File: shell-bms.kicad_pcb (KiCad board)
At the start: 4 copper layers, 184 parts, among them J1 Conn_01x20, J10 Conn_01x05, J11 USB_C_Receptacle_USB2.0_16P, J13 OUTSIDE LED, J2 Conn_01x20, J3 Conn_01x04, J4 Output, J5 USB_C_Receptacle_USB2.0_16P, J6 Conn_01x02, J7 Conn_01x02, J8 Conn_01x02, J9 Conn_01x04, Q1 NPN, Q2 HY3610P, Q3 HY3610P, Q4 BC817, Q5 BC817, Q6 BC817, SW1 SW_Push, SW2 SW_Nidec_CAS-120A1, U1 BQ76952PFBR, U2 LM5017MR, U3 STM32G431C8Tx, U4 AP2204K-5.0, U5 CH340K, U6 XC6206 - 3V3, U7 ESP-WROOM-02, U8 TJA1051T, U9 CH340K, Y1 8MHz

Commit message: finalised product
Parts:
- added Q7: BC817, Package_TO_SOT_SMD:SOT-23, F.Cu at (182.2, 161.2)
- added R72: 260, Resistor_SMD:R_0603_1608Metric_Pad0.98x0.95mm_HandSolder, F.Cu at (181.2, 164.8)
- C10, C11, C12, C13, C14, C15, C16, C17, C2, C3, C4, C42, C43, C45, C47, C5, C52, C53, C54, C59, C6, C60, C7, C8, C9: moved to B.Cu
- JP1: footprint Connector_PinHeader_1.27mm:PinHeader_1x03_P1.27mm_Horizontal -> Connector_PinHeader_1.27mm:PinHeader_1x03_P1.27mm_Vertical
- R18, R19, R20, R21: footprint Resistor_SMD:R_1210_3225Metric_Pad1.30x2.65mm_HandSolder -> Resistor_SMD:R_0603_1608Metric_Pad0.98x0.95mm_HandSolder
- R25, R26, R27, R39: footprint Resistor_THT:R_Axial_DIN0309_L9.0mm_D3.2mm_P15.24mm_Horizontal -> Resistor_SMD:R_1210_3225Metric_Pad1.30x2.65mm_HandSolder
- R31, R37, R38: footprint Resistor_THT:R_Axial_DIN0309_L9.0mm_D3.2mm_P15.24mm_Horizontal -> Resistor_SMD:R_1206_3216Metric
- R60: footprint Resistor_SMD:R_0603_1608Metric_Pad0.98x0.95mm_HandSolder -> Resistor_SMD:R_1206_3216Metric
- R61: footprint Resistor_SMD:R_0603_1608Metric_Pad0.98x0.95mm_HandSolder -> Resistor_SMD:R_1210_3225Metric_Pad1.30x2.65mm_HandSolder
- moved R40 180.9 mm to (241.0, 162.5)
- moved R41 180.9 mm to (241.0, 167.2)
- moved R42 180.9 mm to (241.0, 172.0)
- moved C31 180.9 mm to (266.1, 171.8)
- moved J5 180.9 mm to (263.7, 165.6)
- moved U5 168.1 mm to (228.9, 168.4), turned to 90 degrees
- moved C61 164.8 mm to (41.1, 149.6)
- moved C62 164.8 mm to (62.4, 153.5)
- moved C64 164.8 mm to (65.5, 155.9)
- moved C65 164.8 mm to (73.4, 134.4)
- moved J11 164.8 mm to (73.9, 151.8)
- moved JP2 164.8 mm to (44.9, 138.4)
- moved R64 164.8 mm to (57.7, 139.4)
- moved R65 164.8 mm to (38.7, 149.6)
- moved R68 164.8 mm to (75.1, 145.3)
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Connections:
- C1 pad 1: GND -> GNDPWR
- C17 pad 1: GND -> GNDPWR
- C18 pad 2: GND -> GNDPWR
- C19 pad 2: GND -> GNDPWR
- C20 pad 2: GND -> GNDPWR
- C26 pad 2: GND -> GNDPWR
- C28 pad 1: GND -> GNDPWR
- C38 pad 2: GND -> GNDPWR
- C39 pad 2: GND -> GNDPWR
- C40 pad 2: GND -> GNDPWR
- C41 pad 2: GND -> GNDPWR
- J1 pad 20: GND -> GNDPWR
- JP1 pad 1: /Data_Utils/STAT_LED -> Net-(JP1-A)
- JP2 pad 3: /MCU/esp32/ESP_RX -> /Data_Utils/RXD
- JP3 pad 3: /MCU/esp32/ESP_TX -> /Data_Utils/TXD
- R23 pad 2: GND -> GNDPWR
- R24 pad 2: GND -> GNDPWR
- R45 pad 1: GND -> GNDPWR
- R47 pad 1: Net-(C14-Pad2) -> Net-(U1-VC14)
- R47 pad 2: Net-(U1-VC14) -> Net-(C14-Pad2)
- U1 pad 17: GND -> GNDPWR
- U1 pad 29: GND -> GNDPWR
- U1 pad 30: GND -> GNDPWR
- U4 pad 2: GND -> GNDPWR
- U6 pad 1: GND -> GNDPWR
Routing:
- net Net-(D4-A): track 0.00 -> 85.4 mm, vias 0 -> 2
- net /ReaderIC/Balance-Input/B_0: track 0.00 -> 81.3 mm, vias 0 -> 2
- net /ReaderIC/Balance-Input/B_16: track 0.00 -> 77.1 mm, vias 0 -> 2
- net /ReaderIC/Balance-Input/B_14: track 0.00 -> 73.3 mm, vias 0 -> 2
- net /ReaderIC/Balance-Input/B_12: track 0.00 -> 72.0 mm, vias 0 -> 2
- net /ReaderIC/Balance-Input/B_15: track 0.00 -> 71.2 mm, vias 0 -> 2
- net /ReaderIC/Balance-Input/B_10: track 0.00 -> 70.8 mm, vias 0 -> 2
- net /ReaderIC/Balance-Input/B_13: track 0.00 -> 70.3 mm, vias 0 -> 2
- net /ReaderIC/Balance-Input/B_11: track 0.00 -> 69.4 mm, vias 0 -> 2
- net +12V: track 0.00 -> 68.9 mm
- net /ReaderIC/Balance-Input/B_8: track 0.00 -> 68.8 mm, vias 0 -> 2
- net /ReaderIC/Balance-Input/B_6: track 0.00 -> 68.3 mm, vias 0 -> 2
- net /ReaderIC/Balance-Input/B_4: track 0.00 -> 68.0 mm, vias 0 -> 2
- net /ReaderIC/Balance-Input/B_2: track 0.00 -> 67.4 mm, vias 0 -> 2
- net /ReaderIC/Balance-Input/B_9: track 0.00 -> 66.7 mm, vias 0 -> 2
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- added copper zone on F.Cu, net /Protection/B_Pos
- added copper zone on F.Cu, net /Protection/CD
- added copper zone on B.Cu, net GND
- added copper zone on B.Cu, net GNDPWR
- added copper zone on F.Cu, net GNDPWR
- added copper zone on F.Cu, net Net-(D4-A)
- added copper zone on F.Cu, net Net-(H2-Pad1)

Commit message: near end
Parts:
- C55: moved to B.Cu
- R39: footprint Resistor_SMD:R_1210_3225Metric_Pad1.30x2.65mm_HandSolder -> Resistor_THT:R_Axial_DIN0309_L9.0mm_D3.2mm_P15.24mm_Horizontal
- R40, R41: footprint Resistor_THT:R_Axial_DIN0309_L9.0mm_D3.2mm_P15.24mm_Horizontal -> Resistor_SMD:R_1210_3225Metric_Pad1.30x2.65mm_HandSolder
- R42: footprint Resistor_THT:R_Axial_DIN0309_L9.0mm_D3.2mm_P15.24mm_Horizontal -> Resistor_SMD:R_0603_1608Metric_Pad0.98x0.95mm_HandSolder
- moved R64 199.7 mm to (256.7, 157.0)
- moved C61 199.7 mm to (240.1, 167.2)
- moved C62 199.7 mm to (261.3, 171.1)
- moved C63 199.7 mm to (264.4, 172.0)
- moved C65 199.7 mm to (272.4, 152.0)
- moved J11 199.7 mm to (272.8, 169.5)
- moved R63 199.7 mm to (265.9, 157.0)
- moved R65 199.7 mm to (237.6, 167.2)
- moved R68 199.7 mm to (274.1, 162.9)
- moved R69 199.7 mm to (275.1, 160.1)
- moved R70 199.7 mm to (275.6, 162.8)
- moved R71 199.7 mm to (271.6, 162.9)
- moved SW2 199.7 mm to (261.3, 157.3)
- moved U7 199.7 mm to (250.8, 167.5)
- moved U9 199.7 mm to (277.1, 154.7)
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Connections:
- R50 pad 1: Net-(J6-Pin_2) -> Net-(J6-Pin_1)
- R50 pad 2: Net-(J6-Pin_1) -> Net-(J6-Pin_2)
- U8 pad 6: Net-(J6-Pin_2) -> Net-(J6-Pin_1)
- U8 pad 7: Net-(J6-Pin_1) -> Net-(J6-Pin_2)
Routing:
- net /MCU/NTC: track 0.00 -> 89.5 mm, vias 0 -> 3
- net /Data_Utils/CAN_TX: track 0.00 -> 58.9 mm, vias 0 -> 4
- net /Data_Utils/CAN_RX: track 0.00 -> 58.9 mm, vias 0 -> 4
- net GND: track 31.7 -> 72.6 mm, vias 2 -> 8
- net /MCU/NRST: track 0.00 -> 34.2 mm, vias 0 -> 1
- net Net-(J9-Pin_1): track 0.00 -> 31.7 mm
- net Net-(J9-Pin_2): track 0.00 -> 28.9 mm
- net /Data_Utils/BUZZER: track 0.00 -> 18.7 mm, vias 0 -> 1
- net /Data_Utils/PB3: track 0.00 -> 18.4 mm, vias 0 -> 1
- net /Data_Utils/PB4: track 0.00 -> 16.6 mm, vias 0 -> 1
- net /Data_Utils/USB-: track 0.00 -> 15.5 mm
- net /Data_Utils/PB5: track 0.00 -> 14.3 mm, vias 0 -> 1
- net /Data_Utils/USB+: track 0.00 -> 14.1 mm
- net +3V3: track 27.3 -> 40.5 mm
- net +5V: track 41.5 -> 53.8 mm, vias 0 -> 2
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- added copper zone on In2.Cu, net +3V3
- added copper zone on In1.Cu, net +5V
- added copper zone on In1.Cu, net GND
- added copper zone on In2.Cu, net GND
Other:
- board outline added: 145.3 x 142.3 mm

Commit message: bit artık
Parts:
- removed J4: Output, Connector_AMASS:AMASS_XT60-F_1x02_P7.20mm_Vertical
- added G***: LOGO, LOGO, B.Cu at (149.6, 137.5)
- added H3: MountingHole, Mounting_Wuerth:Mounting_Wuerth_WA-SMST-2.25mm_H2.5mm_9774025943, F.Cu at (69.2, 68.0)
- added H4: MountingHole, Mounting_Wuerth:Mounting_Wuerth_WA-SMST-2.25mm_H2.5mm_9774025943, F.Cu at (169.8, 63.0)
- added H5: MountingHole, Mounting_Wuerth:Mounting_Wuerth_WA-SMST-2.25mm_H2.5mm_9774025943, F.Cu at (121.7, 101.2)
- added H6: MountingHole, Mounting_Wuerth:Mounting_Wuerth_WA-SMST-2.25mm_H2.5mm_9774025943, F.Cu at (108.8, 59.0)
- added MP1: BAT+, WP-BUTR_7460307:WP-BUTR_7460307, F.Cu at (103.9, 73.5)
- added MP2: BAT-, WP-BUTR_7460307:WP-BUTR_7460307, F.Cu at (102.1, 101.2)
- added MP3: PACK+, WP-BUTR_7460307:WP-BUTR_7460307, F.Cu at (159.7, 84.5)
- added MP4: PACK-, WP-BUTR_7460307:WP-BUTR_7460307, F.Cu at (118.0, 86.2)
- added Q8: HY3610P, Package_TO_SOT_THT:TO-220-3_Vertical, F.Cu at (147.1, 57.1)
- added Q9: HY3610P, Package_TO_SOT_THT:TO-220-3_Vertical, F.Cu at (131.3, 58.0)
- C10, C11, C12, C13, C14, C15, C16, C17, C2, C3, C4, C43, C5, C55, C59, C6, C60, C7, C8, C9: moved to F.Cu
- C18, C19, C20, C61, C62, Q4, R62, R63, R64, R65, R66, R67: moved to B.Cu
- H1: value B+ -> MountingHole; footprint MountingHole:MountingHole_8.4mm_M8_Pad_Via -> Mounting_Wuerth:Mounting_Wuerth_WA-SMST-2.25mm_H2.5mm_9774025943
- H2: value B- -> MountingHole; footprint MountingHole:MountingHole_8.4mm_M8_Pad_Via -> Mounting_Wuerth:Mounting_Wuerth_WA-SMST-2.25mm_H2.5mm_9774025943
- J2: footprint Connector_PinSocket_2.54mm:PinSocket_1x20_P2.54mm_Vertical_SMD_Pin1Right -> Connector_PinSocket_2.54mm:PinSocket_1x20_P2.54mm_Horizontal
- R23, R24: footprint Resistor_THT:R_Axial_DIN0309_L9.0mm_D3.2mm_P15.24mm_Horizontal -> Resistor_SMD:R_1210_3225Metric_Pad1.30x2.65mm_HandSolder
- R28, R29: footprint Resistor_THT:R_Axial_DIN0309_L9.0mm_D3.2mm_P15.24mm_Horizontal -> Resistor_SMD:R_1210_3225Metric_Pad1.30x2.65mm_HandSolder; moved to B.Cu
- R51, R52, R53, R56, R58, R59: footprint Resistor_THT:R_Axial_DIN0207_L6.3mm_D2.5mm_P7.62mm_Horizontal -> Resistor_SMD:R_1210_3225Metric_Pad1.30x2.65mm_HandSolder
- R54, R72: footprint Resistor_SMD:R_0603_1608Metric_Pad0.98x0.95mm_HandSolder -> Resistor_SMD:R_1210_3225Metric_Pad1.30x2.65mm_HandSolder
- R57: footprint Resistor_THT:R_Axial_DIN0207_L6.3mm_D2.5mm_P7.62mm_Horizontal -> Resistor_SMD:R_1210_3225Metric_Pad1.30x2.65mm_HandSolder; moved to B.Cu
- moved C64 211.6 mm to (53.1, 165.0)
- moved C63 211.4 mm to (53.1, 167.5)
- moved R67 210.7 mm to (53.4, 157.1)
- moved R63 209.9 mm to (56.3, 167.2), turned to 0 degrees
- moved C62 209.5 mm to (52.5, 153.5)
- moved R62 206.6 mm to (57.1, 159.5), turned to 90 degrees
- moved C65 203.3 mm to (69.2, 156.4), turned to -90 degrees
- moved R69 202.6 mm to (72.5, 157.6), turned to 45 degrees
- moved U9 202.3 mm to (74.8, 153.1), turned to 180 degrees
- moved R71 202.1 mm to (69.5, 159.6), turned to 180 degrees
- moved SW2 201.4 mm to (60.1, 167.0), turned to 90 degrees
- moved J11 200.6 mm to (72.2, 165.4)
- moved R70 200.3 mm to (75.3, 159.8), turned to 180 degrees
- moved R66 199.2 mm to (64.7, 162.2), turned to 180 degrees
- moved R68 197.9 mm to (76.2, 157.2), turned to 180 degrees
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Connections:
- C1 pad 2: /ReaderIC/Balance-Input/B_0 -> Net-(U1-VC0)
- C17 pad 1: GNDPWR -> Net-(U1-VC0)
- C21 pad 1: GND -> GNDPWR
- C22 pad 1: GND -> GNDPWR
- C27 pad 1: GND -> GNDPWR
- C29 pad 1: /Protection/B_Pos -> Net-(D4-A)
- C30 pad 2: Net-(D4-A) -> GNDPWR
- C38 pad 2: GNDPWR -> GND
- C39 pad 2: GNDPWR -> GND
- C40 pad 2: GNDPWR -> GND
- C41 pad 2: GNDPWR -> GND
- C63 pad 2: /MCU/esp32/3V3 -> +3V3
- C64 pad 2: /MCU/esp32/3V3 -> +3V3
- C65 pad 1: /MCU/esp32/3V3 -> +3V3
- H1 pad 1: /Protection/B_Pos -> (no net)
- H2 pad 1: Net-(H2-Pad1) -> (no net)
- J3 pad 4: GND -> GNDPWR
- NT1 pad 3: Net-(H2-Pad1) -> Net-(MP2-Pad1)
- R1 pad 2: /ReaderIC/Balance-Input/B_0 -> Net-(U1-VC0)
- R65 pad 1: /MCU/esp32/3V3 -> +3V3
- R66 pad 1: /MCU/esp32/3V3 -> +3V3
- R67 pad 1: /MCU/esp32/3V3 -> +3V3
- U1 pad 16: /ReaderIC/Balance-Input/B_0 -> Net-(U1-VC0)
- U4 pad 2: GNDPWR -> GND
- U6 pad 1: GNDPWR -> GND
- U7 pad 1: /MCU/esp32/3V3 -> +3V3
- U9 pad 10: /MCU/esp32/3V3 -> +3V3
- U9 pad 7: /MCU/esp32/3V3 -> +3V3
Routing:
- net GND: track 72.6 -> 186.3 mm, vias 8 -> 31
- net Net-(D4-A): track 85.4 -> 2.17 mm, vias 2 -> 0
- net +3V3: track 40.5 -> 111.2 mm, vias 3 -> 37
- net +5V: track 53.8 -> 123.9 mm, vias 2 -> 1
- net /Data_Utils/FAN2: track 0.00 -> 69.9 mm, vias 0 -> 2
- net /Protection/B_Pos: track 63.1 -> 1.22 mm
- net /ReaderIC/Balance-Input/B_12: track 72.0 -> 19.5 mm, vias 2 -> 0
- net /ReaderIC/Balance-Input/B_14: track 73.3 -> 21.2 mm, vias 2 -> 0
- net BAT: track 65.4 -> 13.4 mm, vias 2 -> 0
- net /ReaderIC/Balance-Input/B_10: track 70.8 -> 19.0 mm, vias 2 -> 0
- net /ReaderIC/Balance-Input/B_4: track 68.0 -> 17.3 mm, vias 2 -> 0
- net /ReaderIC/Balance-Input/B_6: track 68.3 -> 17.9 mm, vias 2 -> 0
- net /ReaderIC/Balance-Input/B_8: track 68.8 -> 18.4 mm, vias 2 -> 0
- net /ReaderIC/Balance-Input/B_11: track 69.4 -> 19.2 mm, vias 2 -> 0
- net /ReaderIC/Balance-Input/B_2: track 67.4 -> 17.5 mm, vias 2 -> 0
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- added copper zone on F.Cu, net +12V
- added copper zone on B.Cu, net +3V3
- added copper zone on F.Cu, net +3V3
- added copper zone on B.Cu, net /Protection/B_Pos
- added copper zone on In1.Cu, net /Protection/B_Pos
- added copper zone on F.Cu, net GND
- added copper zone on In1.Cu, net GNDPWR
- added copper zone on F.Cu, net Net-(D3-K)
- added copper zone on F.Cu, net Net-(D4-K)
- added copper zone on F.Cu, net Net-(R33-Pad2)
- added copper zone on F.Cu, net Net-(R35-Pad2)
- removed copper zone on In2.Cu, net +3V3
- removed copper zone on In1.Cu, net +5V
- removed copper zone on B.Cu, net GNDPWR
- removed copper zone on F.Cu, net Net-(H2-Pad1)
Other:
- board size 145.3 x 142.3 mm -> 128.2 x 122.2 mm
- board text added: "0R Dirençler 16S = R20 R21 R47 Bağlı, 15S = R18 R19 R21 R47 Bağlı 14S = R18 R19 R47 R48 Bağlı"
- board text added: "16S - 15S - 14S ALL IN ONE BATTERY MANAGEMENT SYSTEM"
- board text added: "C1 C2 C3 C4 C5 C6 C7 C8 C9 C10 C11 C12 C13 C14 C15 C16 NC NTC+ NTC-"
- board text added: "Cell-"
- board text added: "DESIGNED BY ANSHINX FOR PEHLIVAN TEAM"
- board text added: "PACK+"
- board text added: "PEHLIBMS v0.3"

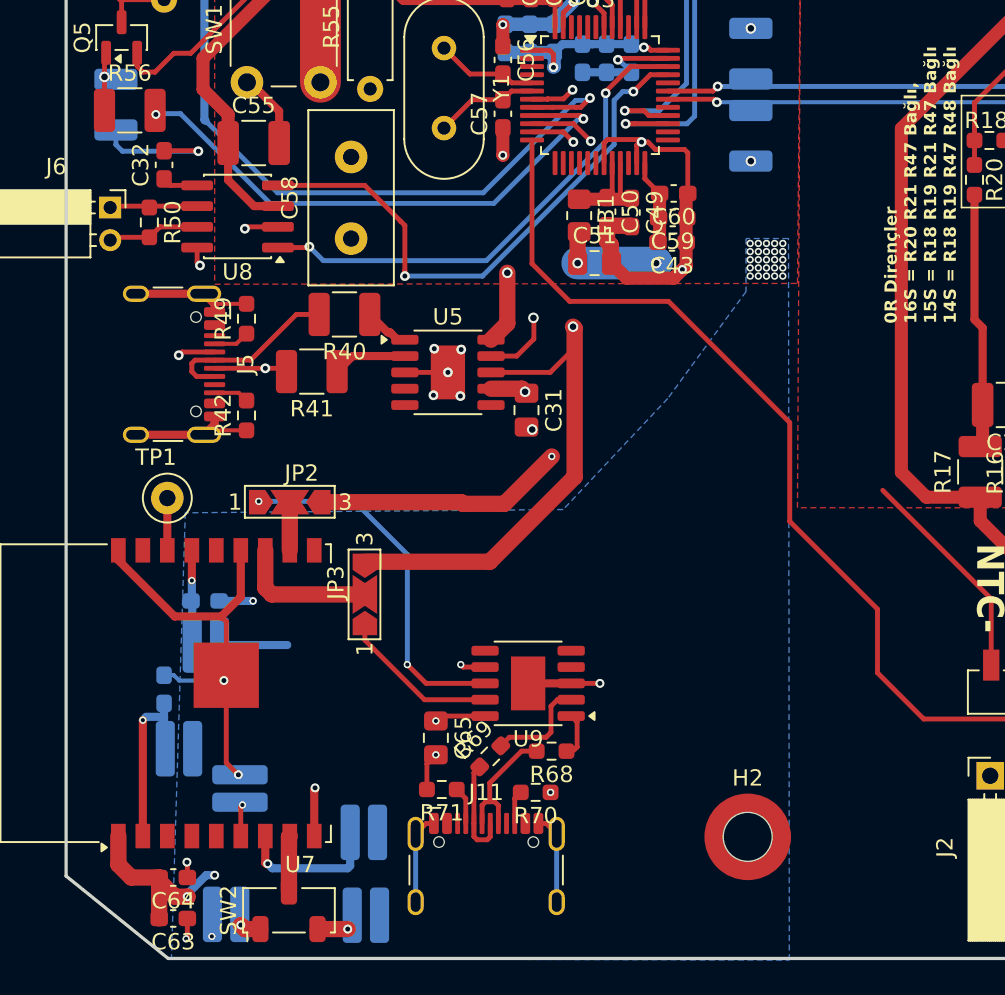
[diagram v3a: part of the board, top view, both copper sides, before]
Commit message: esp-32 layout changes
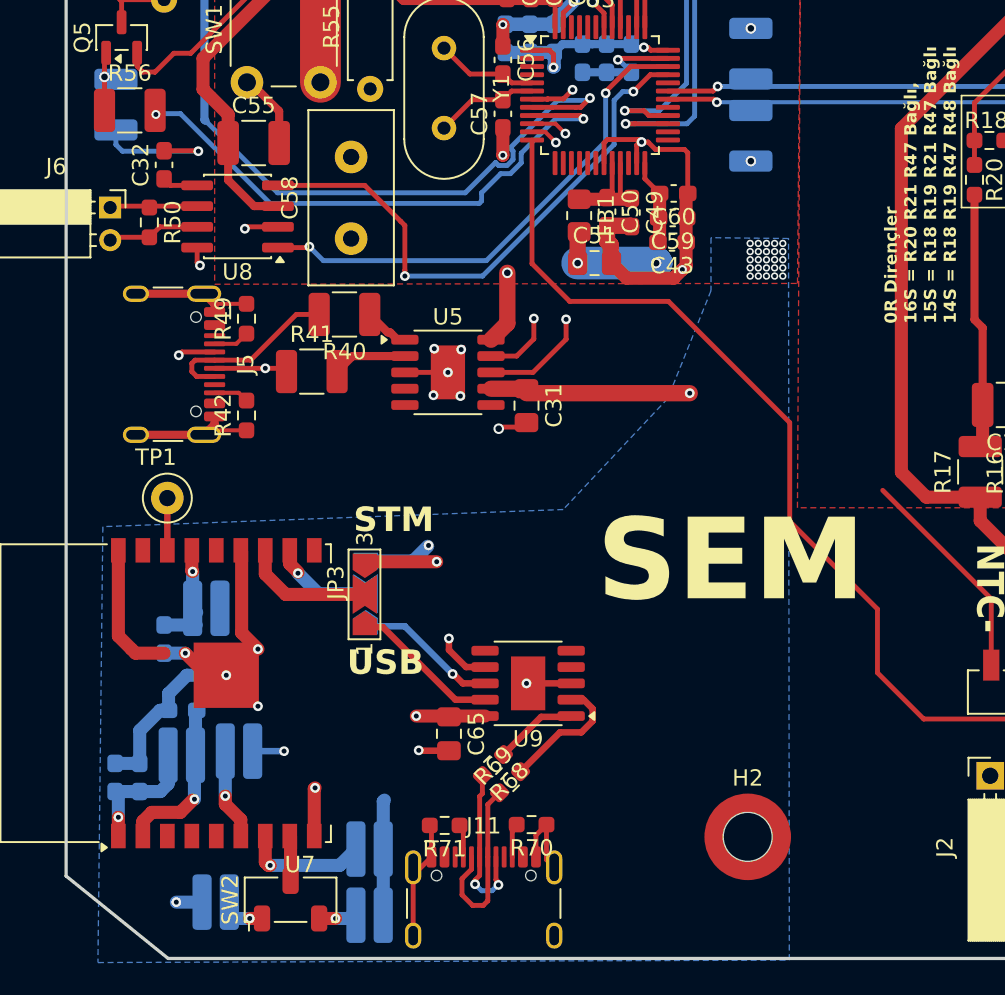
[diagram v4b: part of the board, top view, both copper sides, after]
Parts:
- C63, C64, JP2: moved to B.Cu
- moved C63 9.34 mm to (49.5, 158.9), turned to -90 degrees
- moved JP2 7.28 mm to (64.8, 147.6), turned to 90 degrees
- moved C64 6.46 mm to (51.0, 158.9), turned to -90 degrees
- moved R68 3.69 mm to (72.6, 158.1), turned to -135 degrees
- moved C61 3.43 mm to (52.5, 150.4), turned to -90 degrees
- moved R62 2.29 mm to (57.1, 157.2), turned to 0 degrees
- moved R65 2.25 mm to (55.1, 148.5)
- moved R71 2.21 mm to (69.7, 161.8)
- moved J11 2.06 mm to (72.1, 167.5)
- moved R69 2.00 mm to (73.7, 159.2)
- moved R70 1.99 mm to (75.0, 161.8)
- moved C62 1.72 mm to (53.6, 154.8), turned to 180 degrees
- moved R66 1.08 mm to (65.1, 163.2)
- moved R63 0.98 mm to (55.7, 166.5)
- moved C65 0.84 mm to (70.0, 156.2)
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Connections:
- J5 pad A6: /Data_Utils/USB+ -> Net-(J5-D+-PadA6)
- J5 pad A7: /Data_Utils/USB- -> Net-(J5-D--PadA7)
- J5 pad B6: /Data_Utils/USB+ -> Net-(J5-D+-PadA6)
- J5 pad B7: /Data_Utils/USB- -> Net-(J5-D--PadA7)
- R40 pad 2: /Data_Utils/USB+ -> Net-(J5-D+-PadA6)
- R41 pad 1: /Data_Utils/USB- -> Net-(J5-D--PadA7)
- R68 pad 1: /MCU/esp32/USB+ -> Net-(U9-UD+)
- R69 pad 2: /MCU/esp32/USB- -> Net-(U9-UD-)
- U9 pad 1: /MCU/esp32/USB+ -> Net-(U9-UD+)
- U9 pad 2: /MCU/esp32/USB- -> Net-(U9-UD-)
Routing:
- net Net-(JP2-A): track 22.4 -> 8.76 mm, vias 2 -> 1
- net Net-(J5-D--PadA7): track 0.00 -> 12.7 mm, vias 0 -> 2
- net /Data_Utils/USB-: track 17.2 -> 4.54 mm, vias 2 -> 0
- net Net-(J5-D+-PadA6): track 0.00 -> 11.1 mm
- net /Data_Utils/USB+: track 13.9 -> 2.79 mm
- net +3V3: track 111.2 -> 122.2 mm, vias 37 -> 36
- net /Data_Utils/RXD: track 46.4 -> 38.2 mm
- net Net-(U9-UD-): track 0.00 -> 7.99 mm
- net Net-(U9-UD+): track 0.00 -> 5.12 mm
- net /Data_Utils/TXD: track 47.9 -> 42.9 mm, vias 2 -> 3
- net Net-(U7-IO15): track 2.18 -> 5.59 mm
- net Net-(JP2-C): track 2.95 -> 6.22 mm, vias 0 -> 1
- net /MCU/esp32/USB-: track 13.7 -> 11.4 mm
- net GND: track 186.3 -> 188.2 mm, vias 31 -> 30
- net Net-(SW2-C): track 1.30 -> 3.00 mm
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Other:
- board text added: "SEM"
- board text added: "STM"
- board text added: "USB"
